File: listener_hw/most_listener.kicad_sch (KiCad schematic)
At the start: 149 parts, among them J1 1-1394640-1, J2 ANALYSER, J3 I2S, J4 VBAT_IN, J5 PLR135/T10, J6 PLT133/T10W, J7 RCA 75R, J8 LINE L, J9 LINE R, M1 Tang Nano 20K, M2 ESP32-DevKitC-VIE, U1 74LVC1G34, U10 TPS2553DBVR, U11 74LVC1G123, U12 DIR9001, U13 SRC4192, U14 LP5907MFX-3.3, U15 PCM5102A, U16 LP5907MFX-3.3, U2 74LVC1G157, U3 74LVC1G125, U4 74LVC1G123, U5 TPS7B8133DRV, U6 LMR38020F, U7 Si514, U8 LP5907MFX-3.3, U9 74LVC1G79, X1 24.576MHz

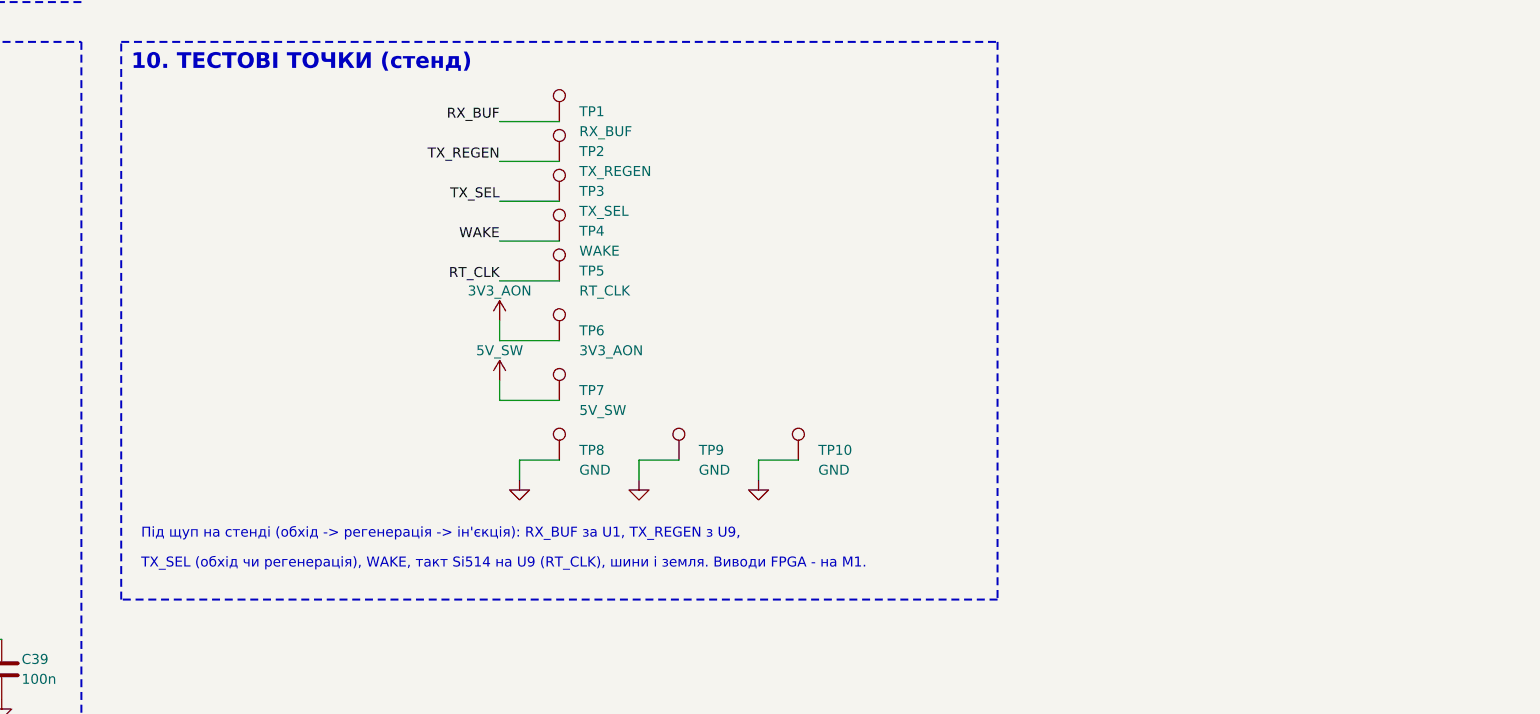
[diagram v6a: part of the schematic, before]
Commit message: Board: narrowed to 123 x 90 mm; TP2 (TX_REGEN) and TP5 (RT_CLK) removed
The user asked for the board to be narrowed and for the probe points on
TX_REGEN and RT_CLK to go: no extra stubs on the regenerator's output into
the ring and on the Si514's clock into U9. Both come out of the sheet
(block 10's note says where the two can still be probed: U9's pins, M1's
TX_FB pin) and off the board; the signal points above J1 now are RX_BUF,
TX_SEL and WAKE, each beside a ground point.

Narrowing: the user had moved H5, J3 and J2 into the free strip right of M2.
Everything else right of the strip - block 9, the coax divider and J7, the
line-out block, the jacks on the right edge, the corner holes - moved 6.75 mm
left, the right edge and both ground pours with it; the jacks stay flush
with the new edge. ERC clean; DRC: no error, no difference from the sheet.

Co-Authored-By: Claude Opus 5.5 <noreply@anthropic.com>
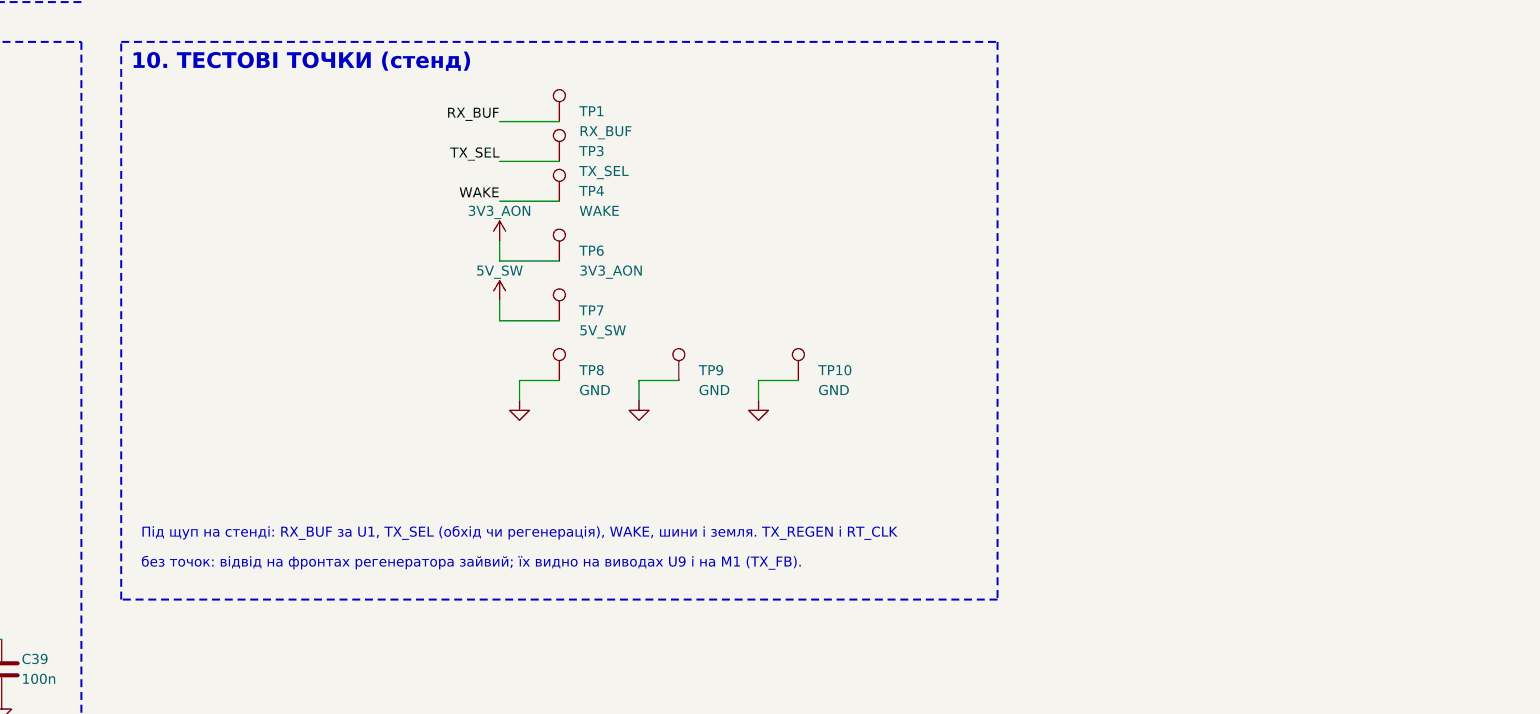
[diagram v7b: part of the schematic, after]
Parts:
- removed TP2: TX_REGEN, TestPoint:TestPoint_Pad_D2.0mm, symbol Connector:TestPoint
- removed TP5: RT_CLK, TestPoint:TestPoint_Pad_D2.0mm, symbol Connector:TestPoint
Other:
- note added: "Під щуп на стенді: RX_BUF за U1, TX_SEL (обхід чи регенерація), WAKE, шини і земля. TX_REGEN і RT_CLK"
- note added: "без точок: відвід на фронтах регенератора зайвий; їх видно на виводах U9 і на M1 (TX_FB)."
- note removed: "TX_SEL (обхід чи регенерація), WAKE, такт Si514 на U9 (RT_CLK), шини і земля. Виводи FPGA - на M1."
- note removed: "Під щуп на стенді (обхід -> регенерація -> ін'єкція): RX_BUF за U1, TX_REGEN з U9,"
- moved on the sheet: TP10, TP3, TP4, TP6, TP7, TP8, TP9

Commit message: Board v1.2: pins swapped on the FPGA and host modules - the bus under M2 runs without a crossing, 33 jumpers instead of 75
- M1: every line bound for the right half leaves the right row in the order it meets J2, J3,
  the DAC and the host; LOCK and S/PDIF swap their LCD-only pins (LOCK on the left row beside
  U11); U13 gets its own copies of BCLK and LRCK (pins 73, 74) and returns DIN2 on 75, over the
  top of the module; PA_EN held low, as the module's amplifier now shares pins 54..56 with J2
- M2: BCLK IO22, LRCK IO23, DIN IO21, UART RX IO4 / TX IO15, OPT_ERR IO13 - on the row that
  faces M1; firmware and its pin table follow
- J2 now 1 SD0, 2 SD1, 3 FS, 4 MCLK, 5 UART_TX, 6 BCLK; J3 now 1 MCLK, 2 DOUT, 3 LRCK, 4 BCLK;
  the silk names every contact; "v1.2" in the silk, rev 1.2 on sheet and board
- the user's fixes: 5V_SW down left of C50 into U16, C50/C51 moved to U16; 3V3_SW into R12
  from below, so SCL/SDA pass between R11 and R12; U7's unused CLK- numbered on one land
  pattern only, so its three pads need no copper
- C23 at U10's input 10u: the host's radio pulses come out of it, not over the 17 cm trunk
- the 33R series resistors under M1 follow their pins; R20/R21 drawn at M2
- checks: DRC no error, no warning, nothing unconnected, matches the sheet; the pin maps of the
  .cst, the top module, the firmware and the sheet agree; Gowin timing PASS (clk_1024
  77.6 MHz, clk_s 119.3 MHz); check_all 24/24, and it now also fails on unconnected items

Co-Authored-By: Claude Opus 5.5 <noreply@anthropic.com>
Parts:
- C23: value 100n -> 10u 16V; footprint Capacitor_SMD:C_0603_1608Metric -> Capacitor_SMD:C_0805_2012Metric
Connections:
- net BCLK_F: now also M1.26 (41 LCD_R4); no longer M1.25 (42 LCD_R3)
- net FS_F: now also M1.30 (48 LCD_DE); no longer M1.26 (41 LCD_R4)
- net I2S_BCLK_F: now also M1.37 (72 HSPI_DIN1), M2.22 (IO22); no longer M1.2 (74 HSPI_DIN3), M2.5 (IO34), U13.25 (BCKO)
- net I2S_DIN2_F: now also M1.3 (75 HSPI_DIR); no longer M1.28 (54 I2S_DIN)
- net I2S_DOUT_F: now also M1.39 (53 EDID_CLK); no longer M1.23 (76 HSPI_DAT)
- net I2S_LRCK_F: now also M1.38 (71 HSPI_DIN0), M2.21 (IO23); no longer M1.3 (75 HSPI_DIR), M2.6 (IO35), U13.24 (LRCKO)
- net I2S_MCLK_F: now also M1.40 (52 EDID_DAT); no longer M1.4 (85 SDIO_D1)
- net LOCK: now also M1.14 (31 LCD_B3); no longer M1.32 (49 LCD_BL)
- net MCLK_F: now also M1.28 (54 I2S_DIN); no longer M1.38 (71 HSPI_DIN0)
- net OPT_ERR: now also M2.15 (IO13); no longer M2.7 (IO32)
- net SD0_F: now also M1.32 (49 LCD_BL); no longer M1.30 (48 LCD_DE)
- net SD1_F: now also M1.31 (55 I2S_LRCK); no longer M1.24 (80 SDIO_D2)
- net SPDIF_F: now also M1.25 (42 LCD_R3); no longer M1.14 (31 LCD_B3)
- net UART_RX_F: now also M1.23 (76 HSPI_DAT); no longer M1.1 (73 HSPI_DIN2)
- net UART_TX_F: now also M1.27 (56 I2S_BCLK), M2.32 (IO4); no longer M1.37 (72 HSPI_DIN1), M2.8 (IO33)
- net at R20.2: now also M2.35 (IO15); no longer M2.9 (IO25)
- net at J3.2 (DOUT): now also R41.2; no longer R39.2
- net at J3.4 (BCLK): now also R39.2; no longer R41.2
- net at R21.2: now also M2.25 (IO21); no longer M2.11 (IO27)
- net at R34.2: now also J2.6 (BCLK); no longer J2.2 (BCLK)
- net at R36.2: now also J2.1 (SD0); no longer J2.4 (SD0)
- net at R37.2: now also J2.2 (SD1); no longer J2.5 (SD1)
- net at R19.2: now also J2.4 (MCLK); no longer J2.1 (MCLK)
- net at R18.2: now also J2.5 (UART_TX); no longer J2.6 (UART_TX)
- new net SRC_BCLK_F: M1.1 (73 HSPI_DIN2), U13.25 (BCKO)
- new net SRC_LRCK_F: M1.2 (74 HSPI_DIN3), U13.24 (LRCKO)
- no-connect marks 63 -> 61
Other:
- note added: "I2S slave: IO22/23 <- BCLK/LRCK, IO21 -> R21 -> DIN; IO13 <- OPT_ERR."
- note added: "OPT_ERR (U12 ERROR) -> M2 IO13: 1 = TOSLINK без сигналу або помилка парності; хост тоді не інжектує. Джерело для інжекції: команда 02, біт M[2]."
- note added: "S/PDIF OUT: SPDIF_F (FPGA 42) -> R28 -> J6 PLT133; R26/R27: 0.5 В на 75 Ом, вихідний опір 75 Ом; C29 без постійної -> J7 RCA. Той самий потік, що й на J3."
- note added: "U13 SRC4192: обидва порти slave (MODE = 000); вхід I2S 24 біт (IFMT = 001) від U12; вихід I2S 24 біт (OFMT = 01, OWL = 00) на тактах FPGA (власні копії BCLK, LRCK: SRC_BCLK_F, SRC_LRCK_F) -> I2S_DIN2_F."
- note added: "UART 3 Мбод: IO4 <- UART_TX, IO15 -> R20 -> UART_RX."
- note added: "v1.2: зв'язки з FPGA - на ряду, що дивиться на M1."
- note added: "v1.2: лінії праворуч - з правого ряду в порядку J2, J3, ЦАП, хост; U13 (SRC_BCLK, SRC_LRCK, DIN2) - з лівого ряду понад модулем."
- note added: "v1.2: порядок контактів J2 і J3 - як їхні виводи на правому ряду M1, доріжки без перехрещень."
- note added: "Кільце і Si514 - лише на виводах LCD (порожній роз'єм): LOCK на 31, S/PDIF на 42. HSPI, 54..56 (входи підсилювача модуля; PA_EN = 51 тримає його вимкненим), EDID 52/53: UART, MCLK, I2S, SD1, DIN2."
- note removed: "I2S slave: IO34/35 <- BCLK/LRCK, IO27 -> DIN; IO32 <- OPT_ERR."
- note removed: "OPT_ERR (U12 ERROR) -> M2 IO32: 1 = TOSLINK без сигналу або помилка парності; хост тоді не інжектує. Джерело для інжекції: команда 02, біт M[2]."
- note removed: "S/PDIF OUT: SPDIF_F (FPGA 31) -> R28 -> J6 PLT133; R26/R27: 0.5 В на 75 Ом, вихідний опір 75 Ом; C29 без постійної -> J7 RCA. Той самий потік, що й на J3."
- note removed: "U13 SRC4192: обидва порти slave (MODE = 000); вхід I2S 24 біт (IFMT = 001) від U12; вихід I2S 24 біт (OFMT = 01, OWL = 00) на тактах FPGA -> I2S_DIN2_F."
- note removed: "UART 3 Мбод: IO33 <- UART_TX, IO25 -> UART_RX."
- note removed: "Кільце і Si514 - лише на виводах LCD (порожній роз'єм); S/PDIF на 31 (LCD_B3). HSPI, TF (80, 85), 54 (I2S_DIN вбудованого ЦАП): UART, MCLK, I2S, SD1, DIN2."
- moved on the sheet: M2, R18, R19, R20, R21, R34, R36, R37, R39, R41
